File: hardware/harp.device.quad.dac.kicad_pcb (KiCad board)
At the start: 4 copper layers, 118.1 x 59.5 mm, 398 parts, among them J1 Conn_01x04_Pin, J11 Conn_Coaxial, J12 Conn_Coaxial, J13 Conn_Coaxial, J14 Conn_Coaxial, J15 Conn_Coaxial, J16 Conn_Coaxial, J17 Conn_Coaxial, J18 Conn_Coaxial, J19 Conn_01x02, J2 Conn_01x03_Male, J20 Conn_01x02, J21 Conn_01x02, J22 Conn_01x02, J23 Conn_01x02, J24 Conn_01x02, J25 Conn_01x02, J26 Conn_01x02, J27 USB_C_Receptacle_USB2.0, J3 USB_C_Receptacle_USB2.0, J4 AudioJack3, J5 Conn_Coaxial, J6 Conn_Coaxial, J7 Conn_Coaxial, J8 Conn_Coaxial, J9 Barrel_Jack_Switch, U1 RP2350B-QFN80, U10 LT1678CS8#PBF, U11 LT1678CS8#PBF, U12 LT1678CS8#PBF, U13 LT1678CS8#PBF, U14 LT1461CIS8-2.5#PBF, U15 LT1678CS8#PBF, U16 LT1678CS8#PBF, U17 LM211DRG4, U18 LM211DRG4, U19 LM211DRG4, U2 LM4040A30IDBZR, U20 LM211DRG4, U21 TXB0102DCT, U22 ADUM4160, U23 74LVCH2T45DC, U24 74LVCH2T45DC, U25 74LVCH2T45DC, U26 LTC3122HMSE#PBF, U27 LTC3115IDHD-2#WPBF, U28 NCP1117-3.3_SOT223, U29 NCP1117-12_SOT223, U3 W25Q128JVS, U30 LM2990SX-12, U31 74LVCH2T45DC, U32 74LVCH2T45DC, U4 W25Q128JVS, U5 W25Q128JVS, U6 LTC2642ACDD-16#PBF, U7 LTC2642ACDD-16#PBF, U8 LTC2642ACDD-16#PBF, U9 LTC2642ACDD-16#PBF

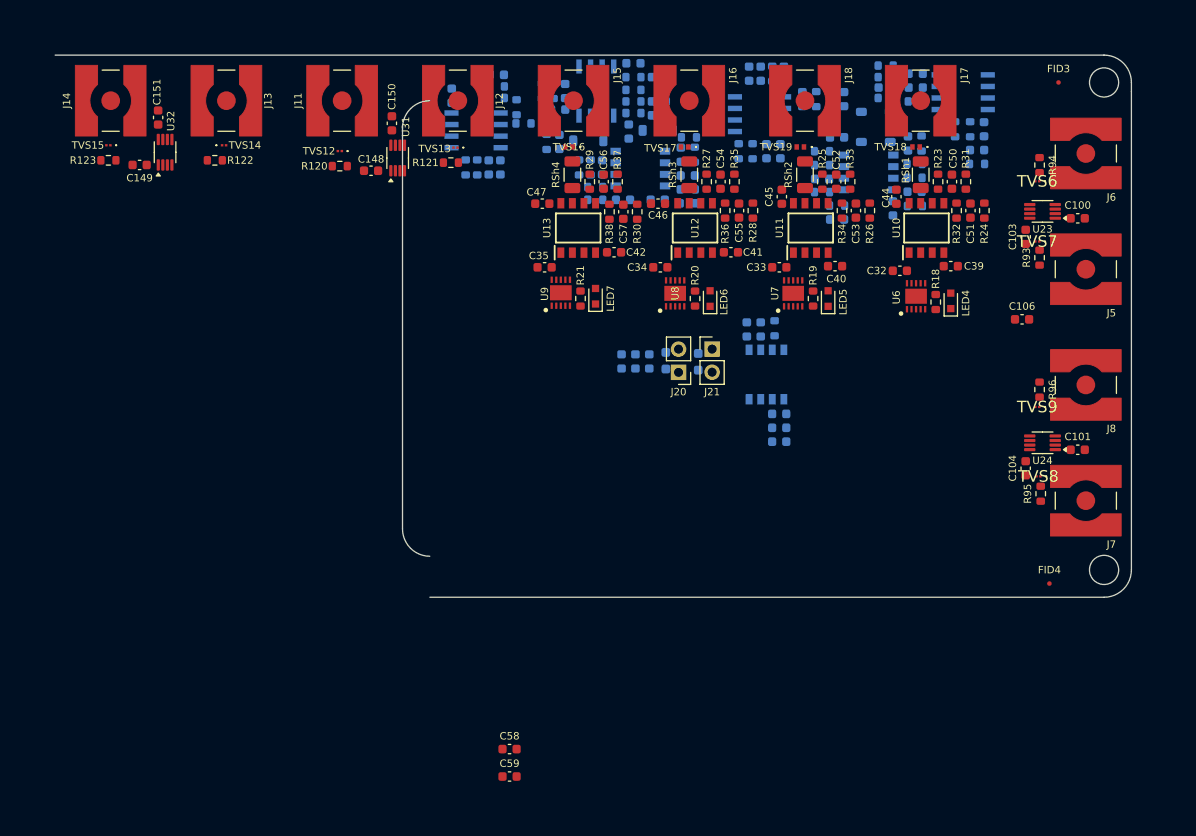
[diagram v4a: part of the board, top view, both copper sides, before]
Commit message: The part designators have been reannotated.
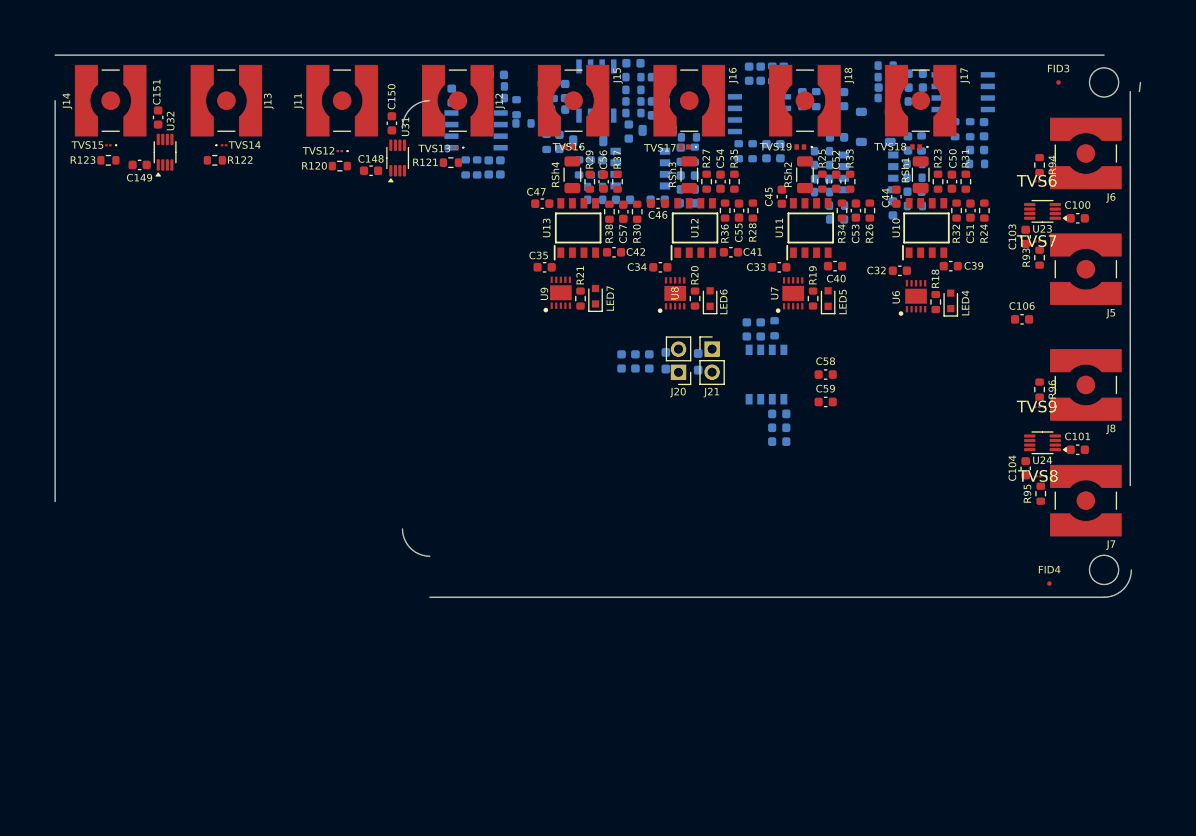
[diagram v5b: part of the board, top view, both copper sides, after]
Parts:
- moved C58 53.8 mm to (225.4, 75.1)
- moved C59 53.8 mm to (225.4, 78.1)
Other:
- board size 118.1 x 59.5 mm -> 119.1 x 59.5 mm
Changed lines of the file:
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@@
 		(allow_soldermask_bridges_in_footprints no)
 		(tenting front back)
-		(grid_origin 235.873 45)
+		(grid_origin 258.873 40)
 		(pcbplotparams
 			(layerselection 0x00000000_00000000_55555555_5755f5ff)
@@
 	(footprint "Capacitor_SMD:C_0603_1608Metric"
 		(layer "F.Cu")
-		(at 190.7495 116.165)
+		(at 225.446 75.057)
 		(descr "Capacitor SMD 0603 (1608 Metric), square (rectangular) end terminal, IPC_7351 nominal, (Body size source: IPC-SM-782 page 76, https://www.pcb-3d.com/wordpress/wp-content/uploads/ipc-sm-782a_amendment_1_and_2.pdf), generated with kicad-footprint-generator")
 		(tags "capacitor")
@@
 	(footprint "Capacitor_SMD:C_0603_1608Metric"
 		(layer "F.Cu")
-		(at 190.7495 119.175)
+		(at 225.446 78.067)
 		(descr "Capacitor SMD 0603 (1608 Metric), square (rectangular) end terminal, IPC_7351 nominal, (Body size source: IPC-SM-782 page 76, https://www.pcb-3d.com/wordpress/wp-content/uploads/ipc-sm-782a_amendment_1_and_2.pdf), generated with kicad-footprint-generator")
 		(tags "capacitor")
@@
 	)
 	(gr_arc
-		(start 256 40)
-		(mid 258.12132 40.87868)
-		(end 259 43)
-		(stroke
-			(width 0.1)
-			(type default)
-		)
-		(layer "Edge.Cuts")
-	)
-	(gr_arc
 		(start 259 96.5)
 		(mid 258.126105 98.616525)
@@
 	)
 	(gr_line
-		(start 179 48)
-		(end 179 92)
+		(start 140.873 45)
+		(end 140.873 89)
 		(stroke
 			(width 0.1)
@@
 	)
 	(gr_line
-		(start 259 96.5)
-		(end 259 44)
+		(start 258.873 87.25)
+		(end 258.873 44)
 		(stroke
 			(width 0.1)
@@
 	)
 	(gr_line
-		(start 259 44)
-		(end 259 43)
+		(start 259.873 44)
+		(end 260 43)
 		(stroke
 			(width 0.1)

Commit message: Some improvements have been made to the layout.
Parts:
- removed D7, D8: BZV55B15, harp.device.quad.dac.kicad:D_MiniMELF
- removed FID4: Fiducial, harp.device.quad.dac.kicad:Fiducial_0.5mm_Mask1mm
- removed J19, J20, J21, J22, J23, J24: Conn_01x02, Connector_PinHeader_2.54mm:PinHeader_1x02_P2.54mm_Vertical
- removed the Jump2 at (207.9, 73.5)
- removed the Jump3 at (211.5, 73.7)
- removed Jump4, Jump5, Jump6, Jump7, Jump8: SolderJumper_2_Open, harp.device.quad.dac.kicad:R_0603_1608Metric_Pad0.98x0.95mm_HandSolder
- removed REF** (x4): MountingHole_3.2mm_M3_DIN965, harp.device.quad.dac.kicad:MountingHole_3.2mm_M3_DIN965
- added H1: MountingHole_Pad, harp.device.quad.dac.kicad:MountingHole_3.2mm_M3_DIN965, F.Cu at (255.9, 43.0)
- added H2: MountingHole_Pad, harp.device.quad.dac.kicad:MountingHole_3.2mm_M3_DIN965, F.Cu at (138.9, 97.0)
- added H3: MountingHole_Pad, harp.device.quad.dac.kicad:MountingHole_3.2mm_M3_DIN965, F.Cu at (138.9, 43.0)
- added H4: MountingHole_Pad, harp.device.quad.dac.kicad:MountingHole_3.2mm_M3_DIN965, F.Cu at (255.9, 97.0)
- added R102: 0, Resistor_SMD:R_0603_1608Metric, B.Cu at (242.7, 95.0)
- added R114: 0, Resistor_SMD:R_0603_1608Metric, F.Cu at (407.9, 168.0)
- added R115: 0, Resistor_SMD:R_0603_1608Metric, F.Cu at (442.9, 233.0)
- added R12: 0, Resistor_SMD:R_0603_1608Metric, F.Cu at (-321.1, -213.0)
- added R23: 0, Resistor_SMD:R_0603_1608Metric, F.Cu at (203.7, 78.0)
- added R24: 0, Resistor_SMD:R_0603_1608Metric, F.Cu at (203.9, 80.0)
- added R88: 0, Resistor_SMD:R_0603_1608Metric, F.Cu at (80.9, -111.0)
- added R89: 0, Resistor_SMD:R_0603_1608Metric, F.Cu at (80.9, -108.5)
- C102, C105, C98, C99, TVS10, U25: moved to B.Cu
- Jump1: value SolderJumper_2_Open -> Conn_01x02; footprint harp.device.quad.dac.kicad:R_0603_1608Metric_Pad0.98x0.95mm_HandSolder -> Connector_PinHeader_2.54mm:PinHeader_1x02_P2.54mm_Vertical
- R97: renamed from R92; moved to B.Cu
- moved J10 329.7 mm to (95.9, 67.0), turned to -90 degrees
- moved C109 316.7 mm to (102.9, 71.0), turned to -90 degrees
- moved R104 316.0 mm to (102.9, 68.0), turned to 0 degrees
- moved R103 315.4 mm to (102.9, 65.0), turned to 0 degrees
- moved C112 314.9 mm to (102.9, 62.0), turned to 90 degrees
- moved J9 314.8 mm to (105.1, 79.2), turned to -90 degrees
- moved C111 307.4 mm to (106.9, 65.0), turned to 180 degrees
- moved C110 307.3 mm to (108.9, 79.0), turned to 90 degrees
- moved TVS11 306.0 mm to (107.9, 68.0), turned to 180 degrees
- moved C107 303.3 mm to (110.9, 79.0), turned to -90 degrees
- moved C108 299.4 mm to (112.9, 79.0), turned to 90 degrees
- moved CMC1 293.5 mm to (115.9, 79.0), turned to 0 degrees
- moved D5 280.2 mm to (120.9, 68.0), turned to -90 degrees
- moved LED9 278.2 mm to (123.9, 80.0), turned to 180 degrees
- moved R113 277.1 mm to (123.9, 77.0), turned to 180 degrees
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- renumbered C110 to C109, C109 to C110, C122 to C121, C124 to C122, C121 to C123, C123 to C124, C129 to C127, C130 to C128, C127 to C129, C132 to C130, C128 to C131, C131 to C132, C135 to C133, C136 to C134, C137 to C135, C138 to C136, C133 to C137, C139 to C138, C140 to C139, C134 to C140, J27 to J10, J26 to Jump2, J25 to Jump3, R95 to R100, R96 to R101, R97 to R103, R98 to R104, R99 to R105, R100 to R106, R101 to R107, R102 to R108, R103 to R109, R104 to R110, R105 to R111, R106 to R112, R107 to R113, R108 to R116, R109 to R117, R111 to R118, R112 to R119, R110 to R120, R113 to R121, R114 to R122, R115 to R123, R116 to R124, R117 to R125, R118 to R126, R119 to R127, R120 to R128, R121 to R129, R12 to R13, R122 to R130, R123 to R131, R13 to R14, R14 to R15, R15 to R16, R16 to R17, R17 to R18, R18 to R19, R19 to R20, R20 to R21, R21 to R22, R22 to R25, R23 to R26, R24 to R27, R25 to R28, R26 to R29, R27 to R30, R28 to R31, R29 to R32, R30 to R33, R31 to R34, R32 to R35, R33 to R36, R34 to R37, R35 to R38, R36 to R39, R37 to R40, R38 to R41, R39 to R42, R40 to R43, R41 to R44, R42 to R45, R43 to R46, R44 to R47, R45 to R48, R46 to R49, R47 to R50, R48 to R51, R49 to R52, R50 to R53, R51 to R54, R52 to R55, R53 to R56, R54 to R57, R55 to R58, R56 to R59, R57 to R60, R58 to R61, R59 to R62, R60 to R63, R61 to R64, R62 to R65, R63 to R66, R64 to R67, R65 to R68, R66 to R69, R67 to R70, R68 to R71, R69 to R72, R70 to R73, R71 to R74, R72 to R75, R73 to R76, R74 to R77, R75 to R78, R76 to R79, R77 to R80, R78 to R81, R79 to R82, R80 to R83, R81 to R84, R82 to R85, R83 to R86, R84 to R87, R85 to R90, R86 to R91, R87 to R92, R88 to R93, R89 to R94, R90 to R95, R91 to R96, R93 to R98, R94 to R99
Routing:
- net +3.3V: track 3.12 -> 0.00 mm
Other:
- board size 119.1 x 59.5 mm -> 123 x 60 mm

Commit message: TVS16,TVS17,TVS18,TVS19 parts have been changed from ESDSB12VLB-TP to PESD12VL1BSLAZ
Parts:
- added Z1: PTV33B-M3_84A, harp.device.quad.dac.kicad:PTV47BM384A, F.Cu at (152.4, 71.3)
- added Z2: PTV5.6B-M3_84A, harp.device.quad.dac.kicad:PTV47BM384A, F.Cu at (167.4, 54.3)
- added Z3: PTV15B-M3_84A, harp.device.quad.dac.kicad:PTV47BM384A, F.Cu at (183.1, 75.6)
- added Z4: PTV15B-M3_84A, harp.device.quad.dac.kicad:PTV47BM384A, F.Cu at (190.7, 72.1)
- C1, C10, C107, C108, C110, C115, C116, C12, C13, C132, C14, C140, C15, C16, C18, C19, C20, C21, C22, C23, C24, C25, C26, C27, C28, C29, C4, C7, C92, C93, CMC1, R1, R103, R104, R109, R110, R111, R112, R114, R115, R118, R119, R120, R121, R122, R123, R13, R14, R15, R23, R24, R3, R4, R5, R86, R87, R88, R89, R91, R92, TVS1, TVS2, TVS3, U21, U28: moved to B.Cu
- C130: value 10pF -> 15pF
- C98, C99, R97: moved to F.Cu
- R10, R11: value 201 -> 220
- R107: value 4.27k -> 4.3k
- R113: value 470 -> 1.10k
- R16, R17, R18, R6, R7, R8: value 10K -> 10k; moved to B.Cu
- R2: value 1K -> 1.10k; moved to B.Cu
- R9: value 27 -> 24; moved to B.Cu
- R90: value 470 -> 330; moved to B.Cu
- RSh1, RSh2, RSh3, RSh4: value CRCW120610R0FKEBC -> RCG120610R0FKEA
- TVS16, TVS17, TVS18, TVS19: value ESDSB12VLB-TP -> PESD12VL1BSLAZ; footprint harp.device.quad.dac.kicad:ESDSB12VLBTP -> harp.device.quad.dac.kicad:PESD12VL1BSLAZ
- moved R12 621.9 mm to (233.6, 68.1)
- moved R11 620.4 mm to (228.3, 75.6), turned to -90 degrees
- moved R10 620.2 mm to (227.1, 75.6), turned to 90 degrees
- moved C17 619.9 mm to (225.8, 75.6), turned to 90 degrees
- moved Jump1 618.5 mm to (229.1, 71.6)
- moved U2 615.9 mm to (230.9, 75.4), turned to 90 degrees
- moved C29 613.6 mm to (229.9, 95.9), turned to 180 degrees
- moved R18 613.6 mm to (229.9, 97.9), turned to 180 degrees
- moved C3 612.5 mm to (215.9, 88.8), turned to 90 degrees
- moved Xtal1 611.3 mm to (218.2, 88.6)
- moved C6 610.5 mm to (214.6, 88.8), turned to 90 degrees
- moved SW4 606.3 mm to (191.8, 98.1)
- moved U5 604.7 mm to (229.6, 96.7)
- moved C9 604.5 mm to (213.3, 88.8), turned to 90 degrees
- moved R5 602.7 mm to (186.7, 98.2)
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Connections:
- R16 pad 1: +3.3V -> /Core_RP2350/QSPI_CS0
- R16 pad 2: /Core_RP2350/QSPI_CS0 -> +3.3V
- R17 pad 1: +3.3V -> /Core_RP2350/QSPI_CS1
- R17 pad 2: /Core_RP2350/QSPI_CS1 -> +3.3V
- R18 pad 1: +3.3V -> /Core_RP2350/QSPI_CS2
- R18 pad 2: /Core_RP2350/QSPI_CS2 -> +3.3V
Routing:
- net /Core_RP2350/QSPI_IO2: track 0.00 -> 61.9 mm
- net /Core_RP2350/QSPI_IO1: track 0.00 -> 60.6 mm
- net /Core_RP2350/QSPI_IO0: track 0.00 -> 56.5 mm
- net /Core_RP2350/QSPI_CLK: track 0.00 -> 52.7 mm
- net /Core_RP2350/QSPI_IO3: track 0.00 -> 46.4 mm
- net /Core_RP2350/QSPI_CS0: track 0.00 -> 43.2 mm, vias 0 -> 2
- net /Core_RP2350/QSPI_CS2: track 0.00 -> 37.4 mm, vias 0 -> 2
- net /Core_RP2350/QSPI_CS1: track 0.00 -> 22.6 mm
- net VBUS: track 16.4 -> 0.00 mm
- net Run_Reset: track 0.00 -> 15.7 mm, vias 0 -> 1
- net SWCLK: track 0.00 -> 13.3 mm, vias 0 -> 1
- net SWDIO: track 0.00 -> 11.2 mm, vias 0 -> 1
- net +3.3V: track 0.00 -> 1.82 mm, vias 0 -> 1
- net DAC3_CS: track 0.00 -> 1.12 mm, vias 0 -> 1
- net /Core_RP2350/Debug_LED2: track 0.00 -> 0.92 mm, vias 0 -> 1
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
